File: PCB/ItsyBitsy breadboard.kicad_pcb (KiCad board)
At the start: 2 copper layers, 63.5 x 22.9 mm, 26 parts, among them J1 EDGE PINS, J2 EDGE PINS, J4 STEMMA, J5 BATTERY, J6 XTRA, J7 BODGE PINS, J8 EDGE PINS, Q1 BSS138DW-7-F, U1 MCP73831-2-OT

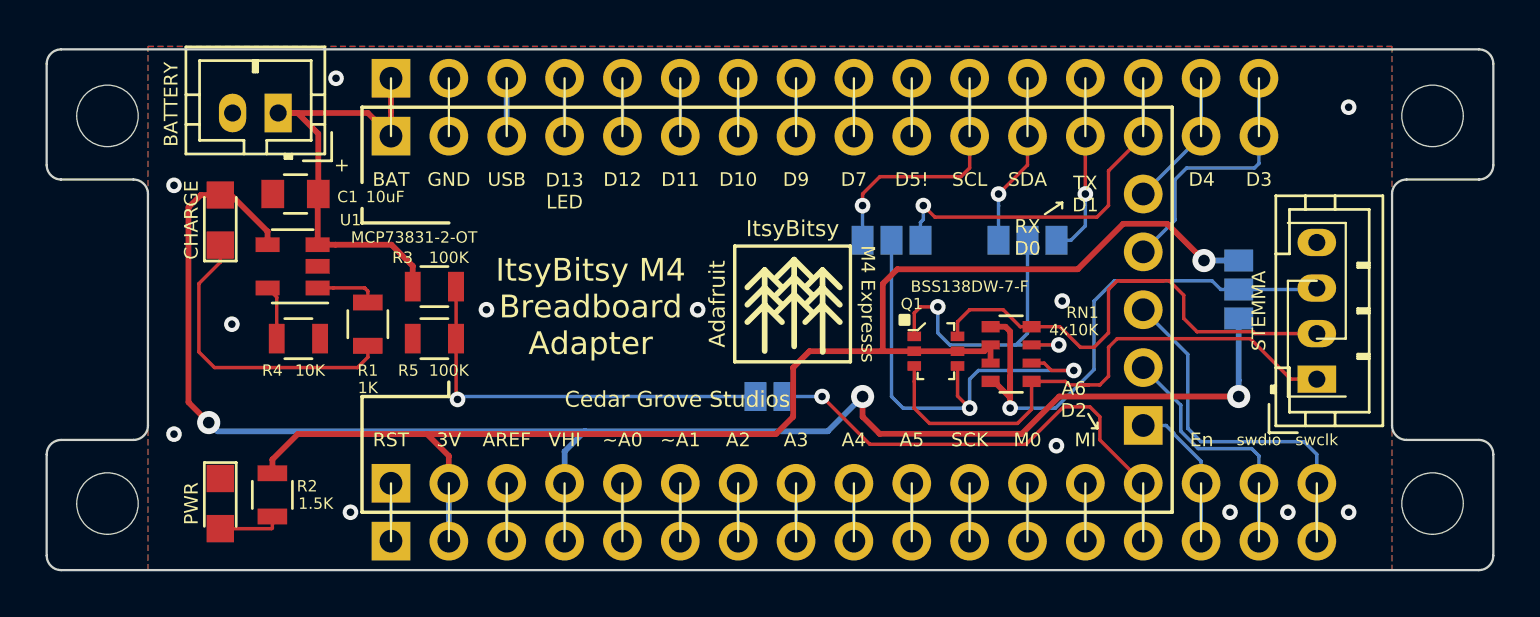
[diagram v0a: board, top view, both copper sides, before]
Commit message: Update STEMMA type default
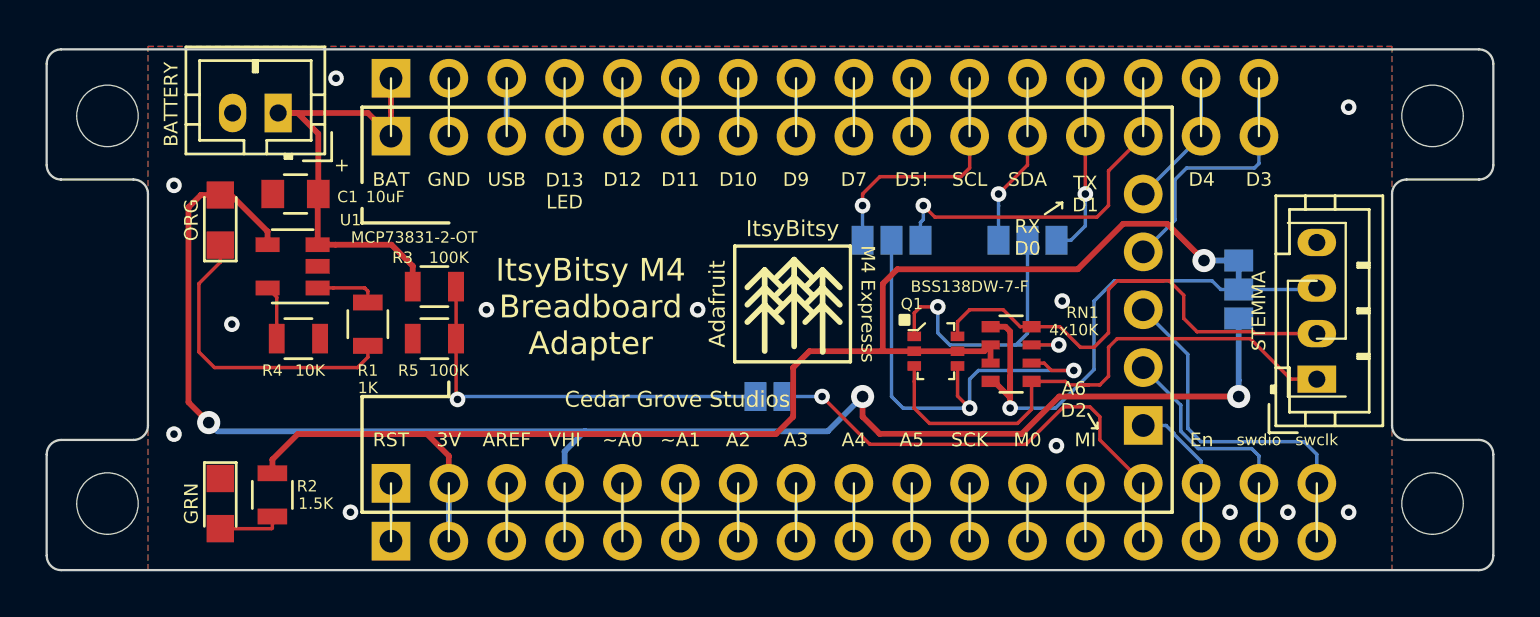
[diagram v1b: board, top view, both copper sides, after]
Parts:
- D1: value CHARGE -> ORG
- D2: value PWR -> GRN
- JMP3: value Vbat -> A6 -> Vbat
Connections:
- J4 pad 3: Net-(J4-Pad3) -> +3V3
- JMP4 pad 2: Net-(J4-Pad3) -> +3V3
- RN1 pad 1: Net-(J4-Pad3) -> +3V3
- RN1 pad 4: Net-(J4-Pad3) -> +3V3
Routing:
- net +3V3: track 61.7 -> 87.5 mm, vias 1 -> 2
- net Net-(J4-Pad3): track 24.5 -> 0.00 mm, vias 1 -> 0
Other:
- board text added: "Vhi"
- board text removed: "5v"
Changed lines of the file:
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@@
   (general
     (thickness 1.6)
-    (drawings 182)
-    (tracks 276)
+    (drawings 183)
+    (tracks 277)
     (zones 0)
     (modules 26)
-    (nets 44)
+    (nets 43)
   )
   (page USLetter)
@@
     (36 B.SilkS user)
     (37 F.SilkS user)
-    (38 B.Mask user hide)
+    (38 B.Mask user)
     (39 F.Mask user hide)
     (40 Dwgs.User user hide)
@@
   (net 41 "Net-(R4-Pad1)")
   (net 42 /SDA_TX)
-  (net 43 "Net-(J4-Pad3)")
   (net_class Default "This is the default net class."
     (clearance 0.1524)
@@
     (add_net "Net-(D1-Pad1)")
     (add_net "Net-(D2-Pad2)")
-    (add_net "Net-(J4-Pad3)")
     (add_net "Net-(JMP3-Pad2)")
     (add_net "Net-(R1-Pad2)")
@@
     (fp_line (start 1.55 1.85) (end -1.55 1.85) (layer F.CrtYd) (width 0.05))
     (pad 1 smd rect (at -0.9 -1.2) (size 0.8 0.5) (layers F.Cu F.Paste F.Mask)
-      (net 43 "Net-(J4-Pad3)"))
+      (net 4 +3V3))
     (pad 3 smd rect (at -0.9 0.4) (size 0.8 0.4) (layers F.Cu F.Paste F.Mask)
       (net 4 +3V3))
@@
       (net 4 +3V3))
     (pad 4 smd rect (at -0.9 1.2) (size 0.8 0.5) (layers F.Cu F.Paste F.Mask)
-      (net 43 "Net-(J4-Pad3)"))
+      (net 4 +3V3))
     (pad 7 smd rect (at 0.9 -0.4) (size 0.8 0.4) (layers F.Cu F.Paste F.Mask)
       (net 42 /SDA_TX))
@@
       (net 37 /STEMMA_SDA))
     (pad 3 thru_hole oval (at 4 0 90) (size 1.2 1.7) (drill 0.75) (layers *.Cu *.Mask)
-      (net 43 "Net-(J4-Pad3)"))
+      (net 4 +3V3))
     (pad 4 thru_hole oval (at 6 0 90) (size 1.2 1.7) (drill 0.75) (layers *.Cu *.Mask)
       (net 1 GND))
@@
       (effects (font (size 0.5 0.5) (thickness 0.1)))
     )
-    (fp_text value CHARGE (at 0 -1.27 90) (layer F.SilkS)
+    (fp_text value ORG (at 0 -1.27 90) (layer F.SilkS)
       (effects (font (size 0.6 0.6) (thickness 0.12)))
     )
@@
       (effects (font (size 0.5 0.5) (thickness 0.1)))
     )
-    (fp_text value PWR (at 0 1.27 270) (layer F.SilkS)
+    (fp_text value GRN (at 0 1.27 270) (layer F.SilkS)
       (effects (font (size 0.6 0.6) (thickness 0.12)))
     )
@@
       (effects (font (size 1 1) (thickness 0.15)) (justify mirror))
     )
-    (fp_text value "Vbat -> A6" (at 1.651 0.127) (layer B.SilkS)
+    (fp_text value Vbat (at 1.651 0.127) (layer B.SilkS)
       (effects (font (size 0.7 0.7) (thickness 0.14)) (justify mirror))
     )
@@
       (net 6 /Vhi))
     (pad 2 smd rect (at 0 0) (size 1.27 0.97) (layers B.Cu B.Paste B.Mask)
-      (net 43 "Net-(J4-Pad3)"))
+      (net 4 +3V3))
     (pad 3 smd rect (at 0 -1.27) (size 1.27 0.97) (layers B.Cu B.Paste B.Mask)
       (net 4 +3V3))
   )
+  (gr_poly (pts (xy 148.336 105.283) (xy 148.336 107.569) (xy 149.606 107.569) (xy 149.606 105.283)) (layer B.Mask) (width 0.15))
   (gr_line (start 110.49 104.14) (end 110.49 103.505) (layer F.SilkS) (width 0.15))
   (gr_line (start 114.3 111.76) (end 114.3 111.125) (layer F.SilkS) (width 0.15))
@@
     (effects (font (size 0.6 0.6) (thickness 0.12)))
   )
-  (gr_text 3.3v (at 148.971 110.109) (layer B.SilkS)
+  (gr_text 3.3v (at 148.971 104.521) (layer B.SilkS)
     (effects (font (size 0.6 0.6) (thickness 0.12)) (justify mirror))
   )
-  (gr_text 5v (at 148.844 104.267) (layer B.SilkS)
+  (gr_text Vhi (at 148.971 109.474) (layer B.SilkS)
     (effects (font (size 0.6 0.6) (thickness 0.12)) (justify mirror))
   )
@@
   (segment (start 136.293407 109.496407) (end 139.192 109.496407) (width 0.1524) (layer B.Cu) (net 42))
   (segment (start 139.192 109.496407) (end 141.074593 109.496407) (width 0.1524) (layer B.Cu) (net 42))
-  (via (at 138.938 112.268) (size 0.6858) (drill 0.3302) (layers F.Cu B.Cu) (net 43))
-  (segment (start 138.938 110.893073) (end 138.938 112.268) (width 0.254) (layer F.Cu) (net 43))
-  (segment (start 138.734666 108.696407) (end 138.080666 108.696407) (width 0.254) (layer F.Cu) (net 43))
-  (segment (start 138.938 108.899741) (end 138.734666 108.696407) (width 0.254) (layer F.Cu) (net 43))
-  (segment (start 138.894259 111.76) (end 138.938 111.76) (width 0.254) (layer F.Cu) (net 43))
-  (segment (start 138.230666 111.096407) (end 138.894259 111.76) (width 0.254) (layer F.Cu) (net 43))
-  (segment (start 138.080666 111.096407) (end 138.230666 111.096407) (width 0.254) (layer F.Cu) (net 43))
-  (segment (start 138.938 112.268) (end 138.938 111.76) (width 0.254) (layer F.Cu) (net 43))
-  (segment (start 138.938 111.76) (end 138.938 108.899741) (width 0.254) (layer F.Cu) (net 43))
-  (segment (start 152.337 107.061) (end 152.4 106.998) (width 0.1524) (layer B.Cu) (net 43))
-  (segment (start 148.971 107.061) (end 152.337 107.061) (width 0.1524) (layer B.Cu) (net 43))
-  (segment (start 138.938 112.268) (end 140.926822 112.268) (width 0.1524) (layer B.Cu) (net 43))
-  (segment (start 148.1836 107.061) (end 148.971 107.061) (width 0.1524) (layer B.Cu) (net 43))
-  (segment (start 142.621 110.573822) (end 142.621 107.569) (width 0.1524) (layer B.Cu) (net 43))
-  (segment (start 142.621 107.569) (end 143.51 106.68) (width 0.1524) (layer B.Cu) (net 43))
-  (segment (start 143.51 106.68) (end 147.8026 106.68) (width 0.1524) (layer B.Cu) (net 43))
-  (segment (start 140.926822 112.268) (end 142.621 110.573822) (width 0.1524) (layer B.Cu) (net 43))
-  (segment (start 147.8026 106.68) (end 148.1836 107.061) (width 0.1524) (layer B.Cu) (net 43))
+  (via (at 138.938 112.268) (size 0.6858) (drill 0.3302) (layers F.Cu B.Cu) (net 4))
+  (segment (start 138.938 110.893073) (end 138.938 112.268) (width 0.254) (layer F.Cu) (net 4))
+  (segment (start 138.734666 108.696407) (end 138.080666 108.696407) (width 0.254) (layer F.Cu) (net 4))
+  (segment (start 138.938 108.899741) (end 138.734666 108.696407) (width 0.254) (layer F.Cu) (net 4))
+  (segment (start 138.894259 111.76) (end 138.938 111.76) (width 0.254) (layer F.Cu) (net 4))
+  (segment (start 138.230666 111.096407) (end 138.894259 111.76) (width 0.254) (layer F.Cu) (net 4))
+  (segment (start 138.080666 111.096407) (end 138.230666 111.096407) (width 0.254) (layer F.Cu) (net 4))
+  (segment (start 138.938 112.268) (end 138.938 111.76) (width 0.254) (layer F.Cu) (net 4))
+  (segment (start 138.938 111.76) (end 138.938 108.899741) (width 0.254) (layer F.Cu) (net 4))
+  (segment (start 152.337 107.061) (end 152.4 106.998) (width 0.1524) (layer B.Cu) (net 4))
+  (segment (start 148.971 107.061) (end 152.337 107.061) (width 0.1524) (layer B.Cu) (net 4))
+  (segment (start 138.938 112.268) (end 140.926822 112.268) (width 0.1524) (layer B.Cu) (net 4))
+  (segment (start 148.1836 107.061) (end 148.971 107.061) (width 0.1524) (layer B.Cu) (net 4))
+  (segment (start 142.621 110.573822) (end 142.621 107.569) (width 0.1524) (layer B.Cu) (net 4))
+  (segment (start 142.621 107.569) (end 143.51 106.68) (width 0.1524) (layer B.Cu) (net 4))
+  (segment (start 143.51 106.68) (end 147.8026 106.68) (width 0.1524) (layer B.Cu) (net 4))
+  (segment (start 140.926822 112.268) (end 142.621 110.573822) (width 0.1524) (layer B.Cu) (net 4))
+  (segment (start 147.8026 106.68) (end 148.1836 107.061) (width 0.1524) (layer B.Cu) (net 4))
+  (segment (start 148.971 105.791) (end 148.971 107.061) (width 0.254) (layer B.Cu) (net 4))
   (zone (net 1) (net_name GND) (layer F.Cu) (hatch edge 0.508)
     (connect_pads (clearance 0.254))

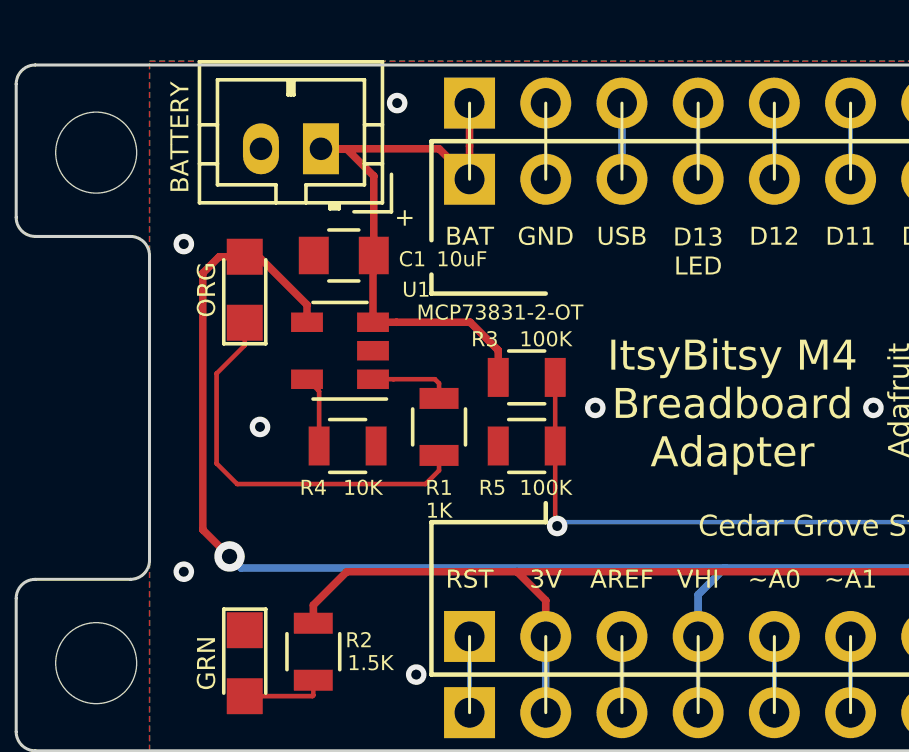
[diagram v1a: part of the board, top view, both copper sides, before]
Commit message: update charging design
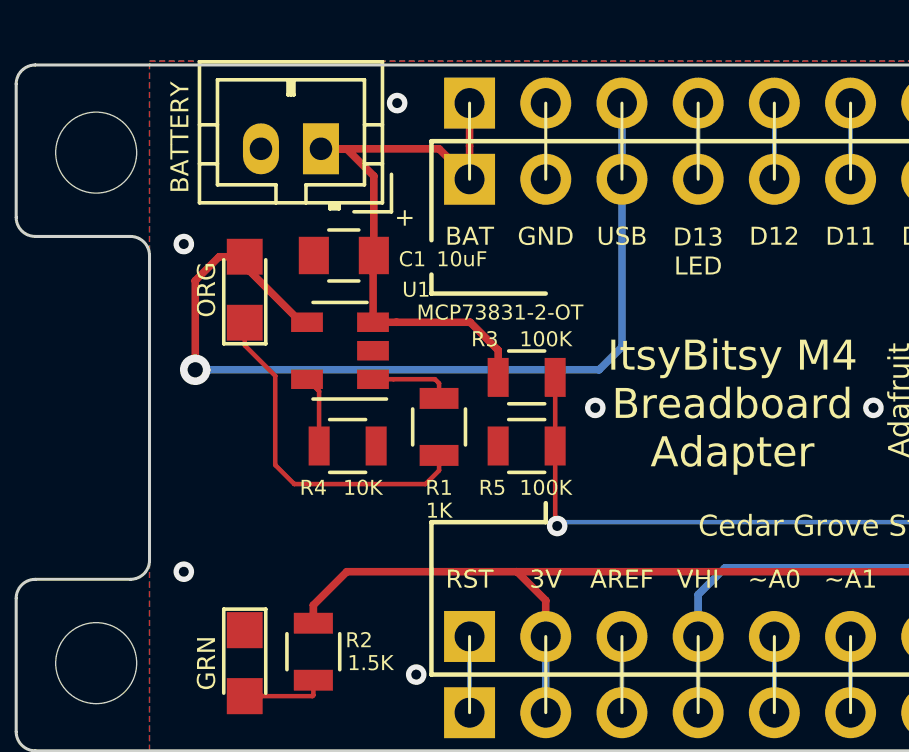
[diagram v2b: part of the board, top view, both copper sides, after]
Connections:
- D1 pad 2: /Vhi -> /USB
- J2 pad 3: +5V -> /USB
- J8 pad 3: +5V -> /USB
- U1 pad 4: /Vhi -> /USB
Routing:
- net /Vhi: track 71.3 -> 39.8 mm, vias 3 -> 2
- net /USB: track 0.00 -> 30.8 mm, vias 0 -> 1
- net +5V: track 2.54 -> 0.00 mm
- net Net-(D1-Pad1): track 13.5 -> 11.6 mm
- net GND: vias 13 -> 12

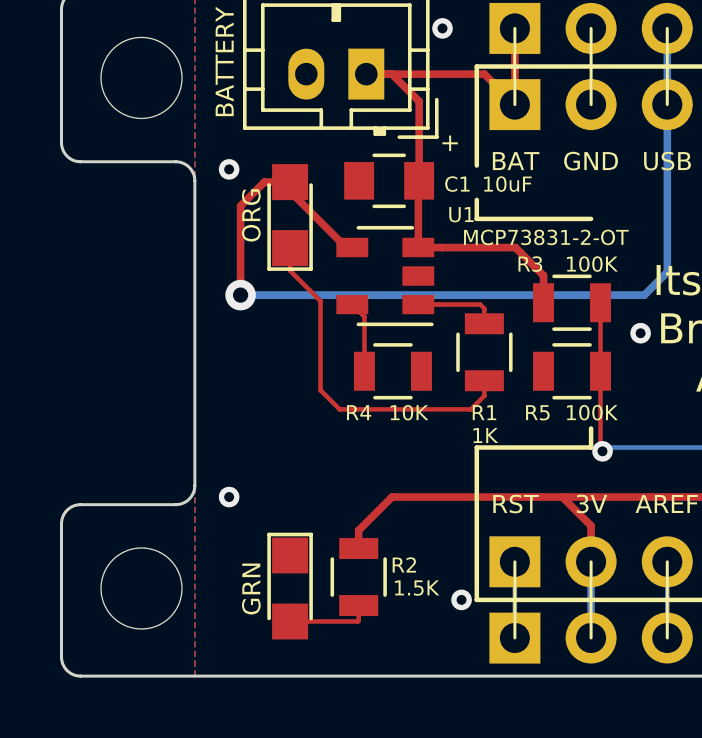
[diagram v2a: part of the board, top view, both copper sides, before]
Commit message: update renderings
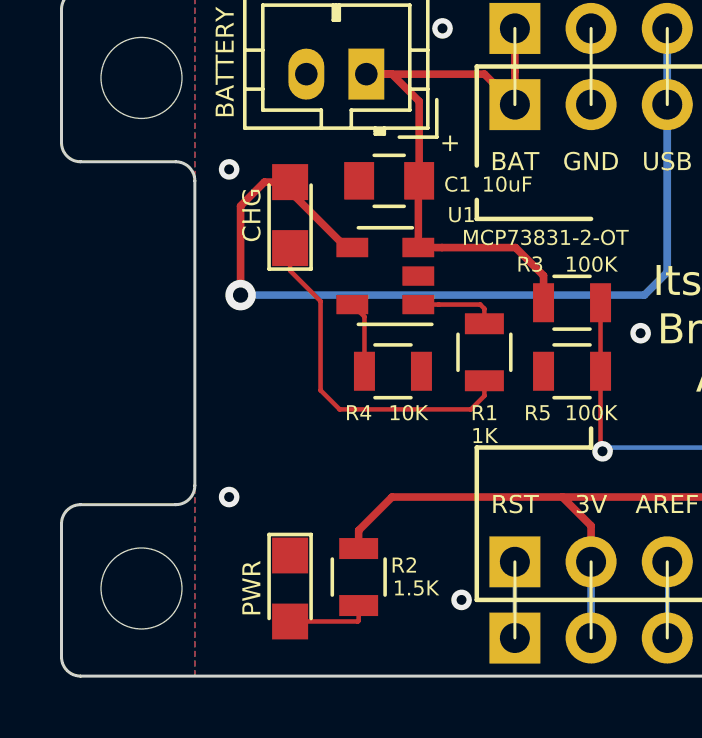
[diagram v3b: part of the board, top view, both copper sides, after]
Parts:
- D1: value ORG -> CHG
- D2: value GRN -> PWR
- JMP3: value Vbat -> Vbat -> A6
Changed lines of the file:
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@@
   (layers
     (0 F.Cu signal)
-    (31 B.Cu signal)
+    (31 B.Cu signal hide)
     (32 B.Adhes user hide)
     (33 F.Adhes user hide)
     (34 B.Paste user hide)
     (35 F.Paste user)
-    (36 B.SilkS user)
+    (36 B.SilkS user hide)
     (37 F.SilkS user)
     (38 B.Mask user)
@@
       (effects (font (size 0.5 0.5) (thickness 0.1)))
     )
-    (fp_text value ORG (at 0 -1.27 90) (layer F.SilkS)
+    (fp_text value CHG (at 0 -1.27 90) (layer F.SilkS)
       (effects (font (size 0.6 0.6) (thickness 0.12)))
     )
@@
       (effects (font (size 0.5 0.5) (thickness 0.1)))
     )
-    (fp_text value GRN (at 0 1.27 270) (layer F.SilkS)
+    (fp_text value PWR (at 0 1.27 270) (layer F.SilkS)
       (effects (font (size 0.6 0.6) (thickness 0.12)))
     )
@@
       (effects (font (size 1 1) (thickness 0.15)) (justify mirror))
     )
-    (fp_text value Vbat (at 1.651 0.127) (layer B.SilkS)
+    (fp_text value "Vbat -> A6" (at 1.651 0.127) (layer B.SilkS)
       (effects (font (size 0.7 0.7) (thickness 0.14)) (justify mirror))
     )
@@
   (segment (start 121.92 100.33) (end 121.92 97.79) (width 0.1524) (layer B.Cu) (net 29))
   (segment (start 119.38 100.33) (end 119.38 97.79) (width 0.1524) (layer B.Cu) (net 30))
-  (segment (start 116.84 100.33) (end 116.84 97.79) (width 0.254) (layer B.Cu) (net 42))
   (segment (start 110.744 99.314) (end 111.76 100.33) (width 0.254) (layer F.Cu) (net 31))
   (segment (start 106.807 99.314) (end 110.744 99.314) (width 0.254) (layer F.Cu) (net 31))
@@
   (segment (start 136.293407 109.496407) (end 139.192 109.496407) (width 0.1524) (layer B.Cu) (net 41))
   (segment (start 139.192 109.496407) (end 141.074593 109.496407) (width 0.1524) (layer B.Cu) (net 41))
+  (segment (start 116.84 100.33) (end 116.84 97.79) (width 0.254) (layer B.Cu) (net 42))
   (segment (start 106.137 105.095) (end 106.342 105.095) (width 0.254) (layer F.Cu) (net 42))
   (segment (start 104.267 103.225) (end 106.137 105.095) (width 0.254) (layer F.Cu) (net 42))

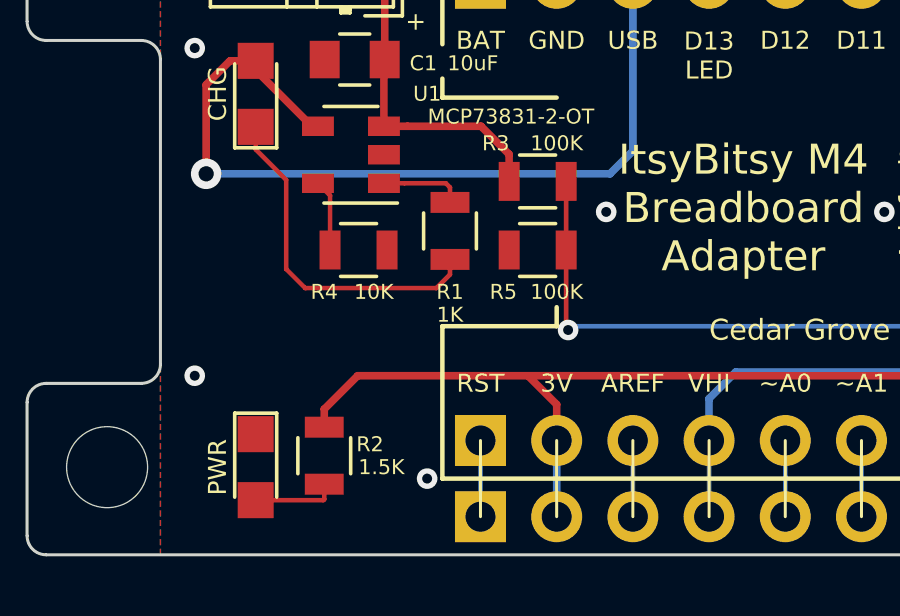
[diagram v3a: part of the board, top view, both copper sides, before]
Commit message: update charging LED resistor
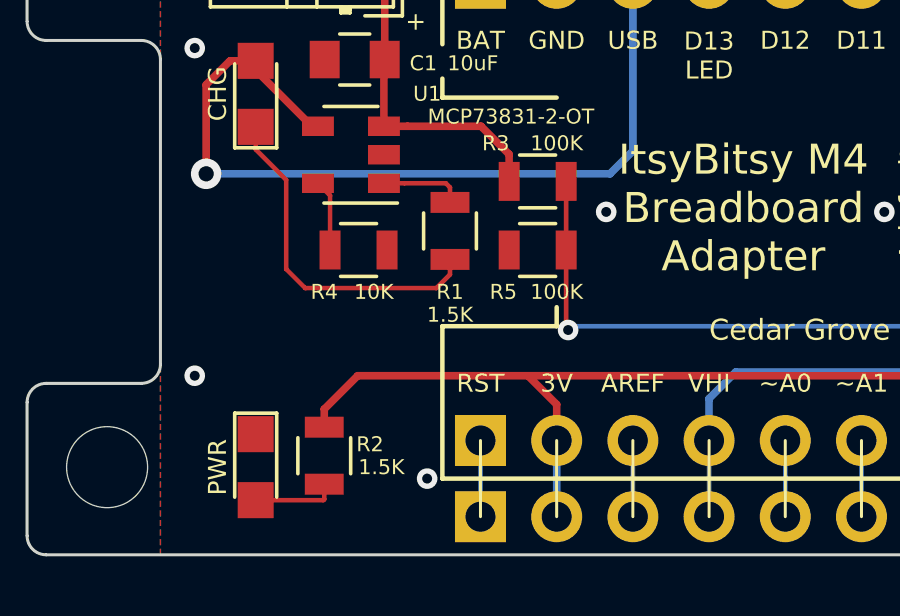
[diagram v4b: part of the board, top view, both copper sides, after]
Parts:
- R1: value 1K -> 1.5K
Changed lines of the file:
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@@
       (effects (font (size 0.5 0.5) (thickness 0.1)))
     )
-    (fp_text value 1K (at -2.794 0 180) (layer F.SilkS)
+    (fp_text value 1.5K (at -2.794 0 180) (layer F.SilkS)
       (effects (font (size 0.5 0.5) (thickness 0.1)))
     )
